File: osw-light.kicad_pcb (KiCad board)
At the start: 4 copper layers, 36.1 x 36.1 mm, 55 parts, among them J1 Conn_01x02, Q1 2N7002, SW1 SW_Push, SW2 SW_Push, SW4 SW_Push, SW5 SW_Push, U1 DS3231MZ, U10 XC6209, U11 MCP73831T-2ACI_OT, U13 XC6209, U2 BMA400, U4 GC9A01_IPS_display, U5 USB-OTG, U6 CH340E, U7 ttgo-32-micro, U9 TPS2115A

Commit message: Starting to add my modifications
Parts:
- removed C4: 0.1u, Capacitor_SMD:C_0603_1608Metric
- removed D1: LED_Green, LED_SMD:LED_0805_2012Metric
- removed G***: LOGO, footprints:p3dt_tiny
- removed G***: LOGO, footprints:aisler_15x12mm
- removed J1: Conn_01x02, Connector_PinHeader_2.54mm:PinHeader_1x02_P2.54mm_Vertical
- removed R13: 470R, Resistor_SMD:R_0603_1608Metric
- removed R15: 5k, Resistor_SMD:R_0603_1608Metric
- removed REF**: OSHW-Logo2_7.3x6mm_SilkScreen, Symbol:OSHW-Logo2_7.3x6mm_SilkScreen
- removed REF**: KiCad-Logo2_5mm_SilkScreen, Symbol:KiCad-Logo2_5mm_SilkScreen
- removed U11: MCP73831T-2ACI_OT, open-Smartwatch:SOT-23-5
- removed U7: ttgo-32-micro, open-Smartwatch:ttgo-32-micro
- removed U9: TPS2115A, open-Smartwatch:TSSOP-8_4.4x3mm_P0.65mm
- added J2: USB_C_Receptacle_USB2.0, Connector_USB:USB_C_Receptacle_GCT_USB4085, F.Cu at (73.1, 113.5)
- added R2: 5k1, Resistor_SMD:R_0603_1608Metric, F.Cu at (82.8, 112.3)
- added R3: 5k1, Resistor_SMD:R_0603_1608Metric, F.Cu at (74.7, 110.7)
- added R5: 10k, Resistor_SMD:R_0603_1608Metric, F.Cu at (65.6, 121.8)
- added TP1: BATT-VCC, TestPoint:TestPoint_Pad_3.0x3.0mm, F.Cu at (61.0, 104.1)
- added TP2: BATT-VCC, TestPoint:TestPoint_Pad_3.0x3.0mm, F.Cu at (61.0, 99.1)
- added U3: ESP32-PICO-MINI-02, open-Smartwatch:ESP32-PICO-MINI-02, F.Cu at (86.4, 101.6)
- C3: value 0.1u -> 1uF
- U1: value DS3231MZ -> RV-8523-C3; footprint Package_SO:SOIC-8_3.9x4.9mm_P1.27mm -> Package_SON:RTC_SMD_MicroCrystal_C3_2.5x3.7mm
- U5: value USB-OTG -> BQ24230RGT; footprint open-Smartwatch:USBmicro-B -> Package_DFN_QFN:VQFN-16-1EP_3x3mm_P0.5mm_EP1.68x1.68mm_ThermalVias
- moved C13 36.5 mm to (46.7, 110.7)
- moved C14 32.6 mm to (41.1, 99.5)
- moved U10 32.6 mm to (40.8, 96.7)
- moved C5 32.6 mm to (40.3, 101.4)
- moved R19 32.6 mm to (41.1, 103.4)
- moved C15 32.6 mm to (36.5, 99.5)
- moved C16 32.6 mm to (41.3, 94.0)
- moved C17 32.6 mm to (36.6, 94.0)
- moved C18 32.6 mm to (41.3, 92.4)
- moved C19 32.6 mm to (36.6, 92.4)
- moved C6 32.6 mm to (35.7, 101.4)
- moved R14 32.6 mm to (38.0, 103.4)
- moved U13 32.6 mm to (36.2, 96.7)
- moved C2 29.4 mm to (42.7, 116.6)
- moved C3 29.4 mm to (45.8, 116.6)
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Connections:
- C1 pad 2: /VBUS -> /VCC
- R14 pad 1: Net-(R14-Pad1) -> GND
- R14 pad 2: GND -> Net-(R14-Pad2)
- U1 pad 1: Net-(U1-Pad1) -> +3V3
- U1 pad 2: +3V3 -> /RTC_INT
- U1 pad 3: /RTC_INT -> /SCL
- U1 pad 4: Net-(U1-Pad4) -> /SDA
- U1 pad 5: GND -> unconnected-(U1-Pad5)
- U1 pad 6: +3V3 -> unconnected-(U1-Pad6)
- U1 pad 7: /SDA -> GND
- U1 pad 8: /SCL -> +3V3
- U10 pad 4: Net-(U10-Pad4) -> unconnected-(U10-Pad4)
- U13 pad 4: Net-(U13-Pad4) -> unconnected-(U13-Pad4)
- U2 pad 11: Net-(U2-Pad11) -> unconnected-(U2-Pad11)
- U2 pad 4: Net-(U2-Pad4) -> unconnected-(U2-Pad4)
- U5 pad 1: GND -> Net-(R5-Pad1)
- U5 pad 2: Net-(U5-Pad2) -> /VBAT
- U5 pad 3: /D_P -> /VBAT
- U5 pad 4: /D_N -> GND
- U5 pad 5: /VBUS -> GND
- U6 pad 4: Net-(U6-Pad4) -> unconnected-(U6-Pad4)
- U6 pad 5: Net-(U6-Pad5) -> unconnected-(U6-Pad5)
- U6 pad 6: Net-(U6-Pad6) -> unconnected-(U6-Pad6)
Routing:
- net +3V3: track 126.3 -> 13.5 mm, vias 11 -> 0
- net GND: track 64.5 -> 0.00 mm, vias 65 -> 0
- net /SCL: track 35.5 -> 0.00 mm, vias 3 -> 0
- net /VCC: track 30.7 -> 0.00 mm
- net /TFT_RST: track 29.6 -> 0.00 mm, vias 2 -> 0
- net /VBAT: track 29.5 -> 0.00 mm, vias 2 -> 0
- net /MOSI: track 28.4 -> 0.00 mm, vias 2 -> 0
- net /SDA: track 28.4 -> 0.00 mm, vias 3 -> 0
- net /B_MON: track 26.9 -> 0.00 mm, vias 2 -> 0
- net /EN: track 25.2 -> 0.00 mm, vias 6 -> 0
- net /BTN3: track 22.8 -> 0.00 mm, vias 3 -> 0
- net /VBUS: track 22.4 -> 0.00 mm
- net /SCK: track 22.0 -> 0.00 mm, vias 1 -> 0
- net /TFT_CS: track 20.6 -> 0.00 mm, vias 2 -> 0
- net /FLASH: track 20.0 -> 0.00 mm, vias 2 -> 0
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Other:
- net class Default removed

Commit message: Finalized layout
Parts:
- added C4: 0.1u, Capacitor_SMD:C_0603_1608Metric, F.Cu at (79.0, 84.8)
- added C7: 220nF, Capacitor_SMD:C_0603_1608Metric, F.Cu at (79.5, 89.4)
- added G***: LOGO, open-Smartwatch:new_707_logo_10x11, B.Cu at (88.9, 101.6)
- added G***: LOGO, footprints:p3dt_tiny, B.Cu at (76.2, 88.6)
- added REF**: KiCad-Logo2_6mm_SilkScreen, Symbol:KiCad-Logo2_6mm_SilkScreen, B.Cu at (76.2, 105.4)
- added U7: LSM303C, Package_LGA:LGA-12_2x2mm_P0.5mm, F.Cu at (79.5, 87.4)
- moved R19 43.1 mm to (82.5, 91.3), turned to 180 degrees
- moved C13 37.7 mm to (78.9, 91.0), turned to 0 degrees
- moved C6 34.2 mm to (69.8, 102.5), turned to 180 degrees
- moved C5 34.1 mm to (74.4, 102.5)
- moved C14 34.1 mm to (75.2, 100.5)
- moved C15 34.1 mm to (70.6, 100.5)
- moved U10 34.1 mm to (74.9, 97.7)
- moved U13 34.1 mm to (70.3, 97.7)
- moved C16 33.6 mm to (74.8, 94.7)
- moved C18 33.6 mm to (74.8, 93.2)
- moved C17 33.5 mm to (70.1, 94.7)
- moved C19 33.5 mm to (70.1, 93.2)
- moved R14 30.0 mm to (67.8, 106.7), turned to -90 degrees
- moved C3 27.2 mm to (70.7, 105.5)
- moved C2 23.7 mm to (64.3, 106.7), turned to 90 degrees
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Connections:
- R19 pad 1: /VCC -> +3V3
- SW2 pad 1: /BTN3 -> +3V3
- SW2 pad 2: +3V3 -> /BTN3
- U2 pad 5: /IO34 -> /IO35
- U2 pad 6: /IO35 -> /IO34
- U3 pad 6: /STAT_PWR -> /DRDY_MAG
- U3 pad 7: unconnected-(U3-Pad7) -> /STAT_PWR
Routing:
- net +3V3: track 13.5 -> 103.5 mm, vias 0 -> 6
- net /SCL: track 0.00 -> 49.3 mm, vias 0 -> 4
- net /SDA: track 0.00 -> 44.4 mm, vias 0 -> 5
- net /VCC: track 0.00 -> 40.4 mm, vias 0 -> 3
- net /STAT_PWR: track 0.00 -> 36.4 mm, vias 0 -> 3
- net /TFT_CS: track 0.00 -> 34.4 mm, vias 0 -> 2
- net /BTN2: track 0.00 -> 33.3 mm, vias 0 -> 2
- net /MOSI: track 0.00 -> 31.2 mm, vias 0 -> 2
- net /VBAT: track 0.00 -> 30.2 mm, vias 0 -> 2
- net /FLASH: track 0.00 -> 28.2 mm, vias 0 -> 2
- net /PIN_LED: track 0.00 -> 27.4 mm, vias 0 -> 2
- net /TFT_RST: track 0.00 -> 27.1 mm, vias 0 -> 2
- net /SCK: track 0.00 -> 27.0 mm, vias 0 -> 2
- net /TFT_DC: track 0.00 -> 26.1 mm, vias 0 -> 2
- net /EN: track 0.00 -> 23.6 mm, vias 0 -> 2
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
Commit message: Started working on LoRa version/changes
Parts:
- removed REF**: KiCad-Logo2_6mm_SilkScreen, Symbol:KiCad-Logo2_6mm_SilkScreen
- added AE1: Antenna, Connector_Coaxial:U.FL_Molex_MCRF_73412-0110_Vertical, F.Cu at (69.8, 93.2)
- added AE2: Antenna, Connector_PinHeader_2.54mm:PinHeader_1x01_P2.54mm_Vertical, F.Cu at (76.2, 84.8)
- added C10: 0.1u, Capacitor_SMD:C_0603_1608Metric, B.Cu at (83.9, 90.2)
- added U8: RFM95W-868S2, RF_Module:HOPERF_RFM9XW_SMD, B.Cu at (83.0, 101.0)
- moved R18 7.87 mm to (79.8, 96.0), turned to 90 degrees
- moved C19 6.52 mm to (65.8, 98.0), turned to 135 degrees
- moved C17 3.84 mm to (66.9, 96.9), turned to 135 degrees
- moved G*** 3.81 mm to (85.1, 101.6)
- moved U1 2.37 mm to (74.8, 89.1)
- moved C11 2.37 mm to (72.1, 88.3)
- moved R21 2.07 mm to (61.3, 95.5)
- moved Q1 2.07 mm to (62.2, 99.0)
- moved R22 2.07 mm to (63.0, 95.5)
- moved C4 0.77 mm to (79.8, 85.0)
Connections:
- U3 pad 19: /TFT_DC -> /MISO
- U3 pad 21: unconnected-(U3-Pad21) -> /TFT_DC
- U3 pad 26: unconnected-(U3-Pad26) -> /LORA_IO0
- U3 pad 27: unconnected-(U3-Pad27) -> /LORA_CS
- U3 pad 28: unconnected-(U3-Pad28) -> /LORA_RST
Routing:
- net /SCL: track 49.3 -> 1.73 mm, vias 4 -> 0
- net +3V3: track 103.5 -> 72.2 mm, vias 6 -> 3
- net /SDA: track 44.4 -> 14.0 mm, vias 5 -> 0
- net /TFT_DC: track 26.1 -> 4.87 mm, vias 2 -> 0
- net /MISO: track 0.00 -> 21.3 mm, vias 0 -> 1
- net /DRDY_MAG: track 17.9 -> 0.00 mm, vias 2 -> 0
- net /EN: track 23.6 -> 7.30 mm, vias 2 -> 1
- net /RTC_INT: track 20.0 -> 5.28 mm, vias 2 -> 1
- net GND: track 19.9 -> 9.69 mm, vias 39 -> 30
- net /STAT_PWR: track 36.4 -> 29.4 mm, vias 3 -> 2
- net /BTN3: track 12.1 -> 7.92 mm
- net /3V3_2: track 16.9 -> 13.5 mm
- net /TFT_RST: track 27.1 -> 30.5 mm
- net /TFT_CS: track 34.4 -> 37.2 mm, vias 2 -> 1
- net /MOSI: track 31.2 -> 34.0 mm
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
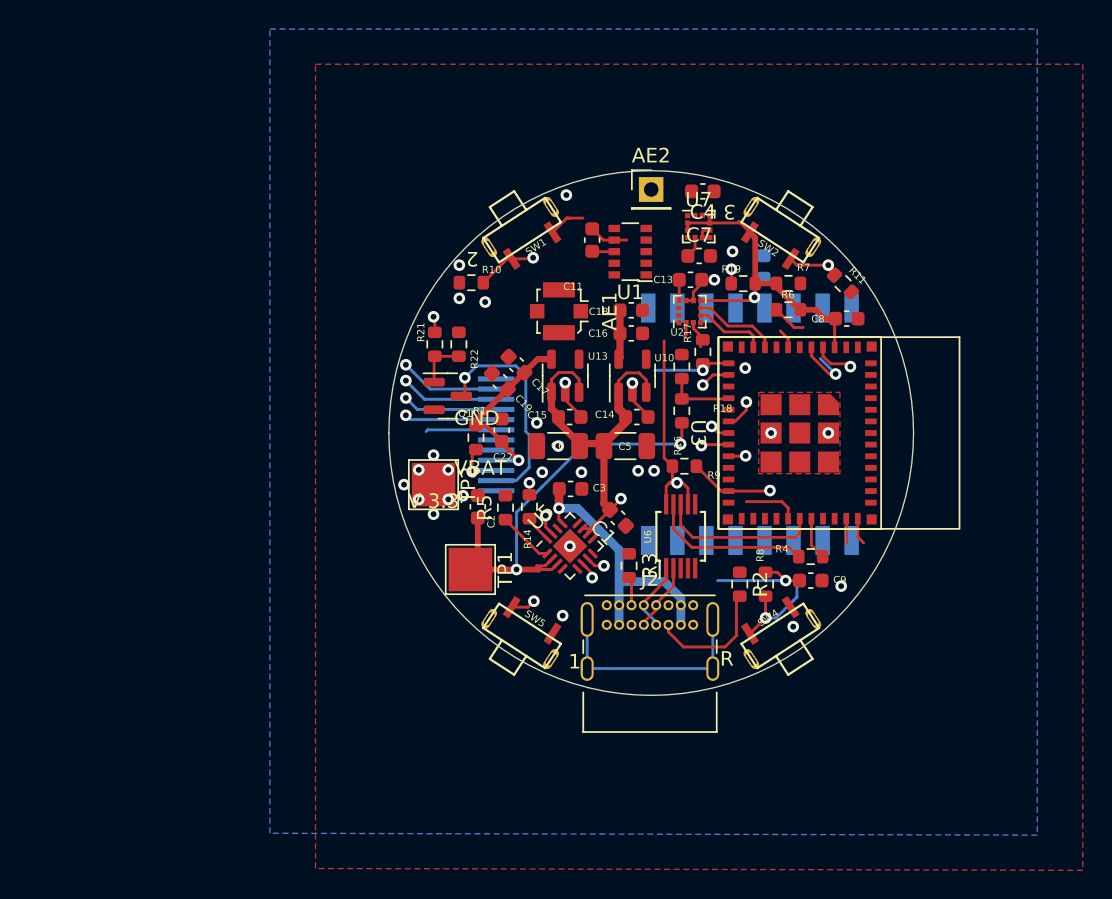
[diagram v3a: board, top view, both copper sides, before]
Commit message: Layed out board. Changed a duplicate sensor for a temperature one
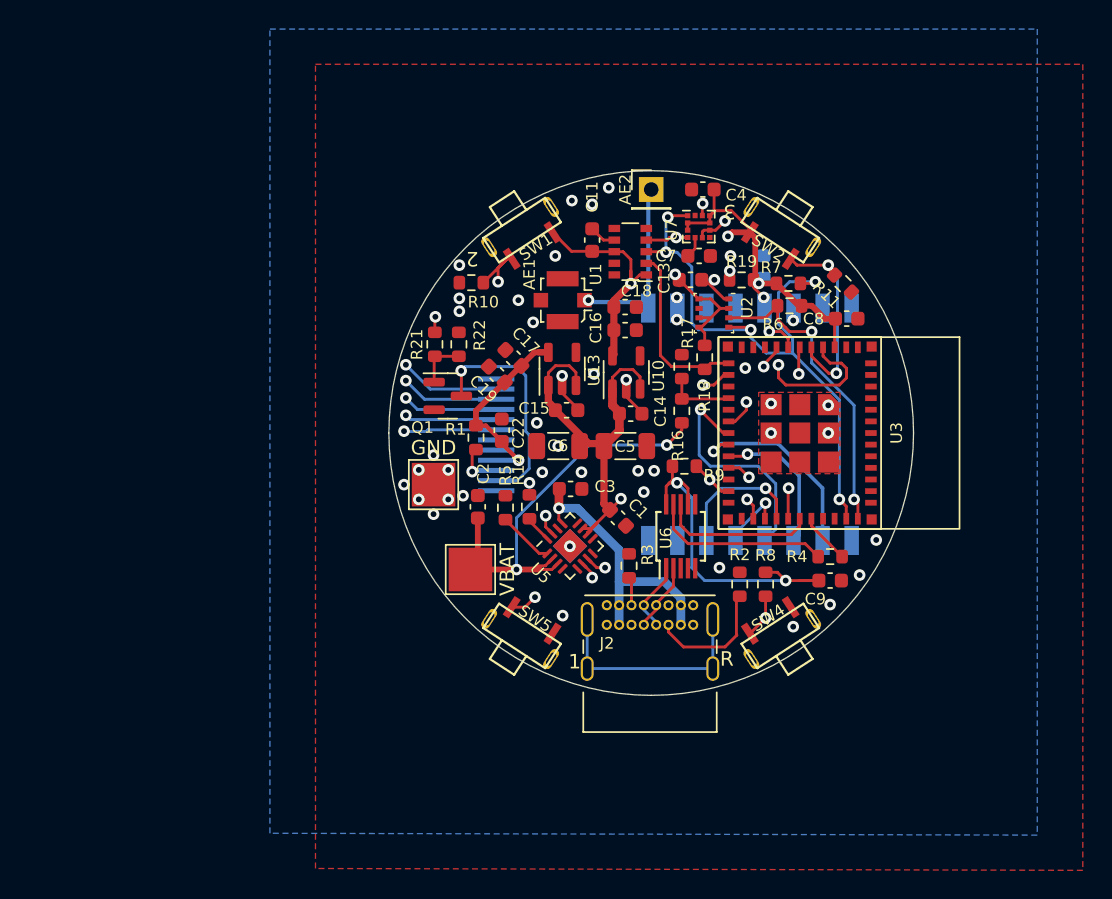
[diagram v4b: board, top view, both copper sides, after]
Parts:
- J2: value USB_C_Receptacle_USB2.0 -> GCT_USB4085
- U2: value BMA400 -> BME280; footprint open-Smartwatch:LGA-12_2x2mm_P0.5mm -> Package_LGA:Bosch_LGA-8_2.5x2.5mm_P0.65mm_ClockwisePinNumbering
- moved U2 1.67 mm to (80.5, 93.3), turned to -90 degrees
- moved C9 1.33 mm to (88.5, 111.8)
- moved R4 1.33 mm to (88.5, 110.1)
- moved G*** 1.02 mm to (86.1, 101.6)
- moved AE1 0.80 mm to (70.1, 92.5)
- moved C15 0.52 mm to (70.4, 100.0)
- moved C17 0.52 mm to (66.7, 96.4)
- moved C19 0.52 mm to (65.6, 97.6)
- moved U13 0.52 mm to (70.1, 97.2)
- moved C16 0.48 mm to (74.4, 94.5)
- moved C14 0.48 mm to (74.8, 100.3)
- moved C18 0.48 mm to (74.4, 92.9)
- moved U10 0.48 mm to (74.5, 97.4)
- moved R18 0.40 mm to (79.9, 96.4)
- moved R6 0.29 mm to (85.7, 92.8)
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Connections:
- AE1 pad 2: (no net) -> GND
- U2 pad 2: /SDA -> +3V3
- U2 pad 3: +3V3 -> /SDA
- U2 pad 4: unconnected-(U2-Pad4) -> /SCL
- U2 pad 5: /IO35 -> +3V3
- U2 pad 6: /IO34 -> +3V3
- U2 pad 7: +3V3 -> GND
- U2 pad 8: GND -> +3V3
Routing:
- net /SCL: track 1.73 -> 42.5 mm, vias 0 -> 5
- net /TFT_DC: track 4.87 -> 33.1 mm, vias 0 -> 2
- net +3V3: track 72.2 -> 100.0 mm, vias 3 -> 7
- net /SDA: track 14.0 -> 39.6 mm, vias 0 -> 3
- net /LORA_IO0: track 0.00 -> 19.4 mm, vias 0 -> 2
- net /DRDY_MAG: track 0.00 -> 18.2 mm, vias 0 -> 2
- net /EN: track 7.30 -> 25.4 mm, vias 1 -> 2
- net /SCK: track 29.8 -> 44.2 mm
- net Net-(AE1-Pad1): track 0.00 -> 13.4 mm, vias 0 -> 1
- net /LORA_RST: track 0.00 -> 9.47 mm, vias 0 -> 1
- net /MOSI: track 34.0 -> 43.1 mm
- net /MISO: track 21.3 -> 13.8 mm
- net /RTC_INT: track 5.28 -> 11.9 mm, vias 1 -> 0
- net /BTN3: track 7.92 -> 14.2 mm
- net /IO34: track 5.88 -> 0.00 mm
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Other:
- board text added: "OpenSmartWatch E707 LORA Edition Rev 1.0"
- board text removed: "V 3.3"

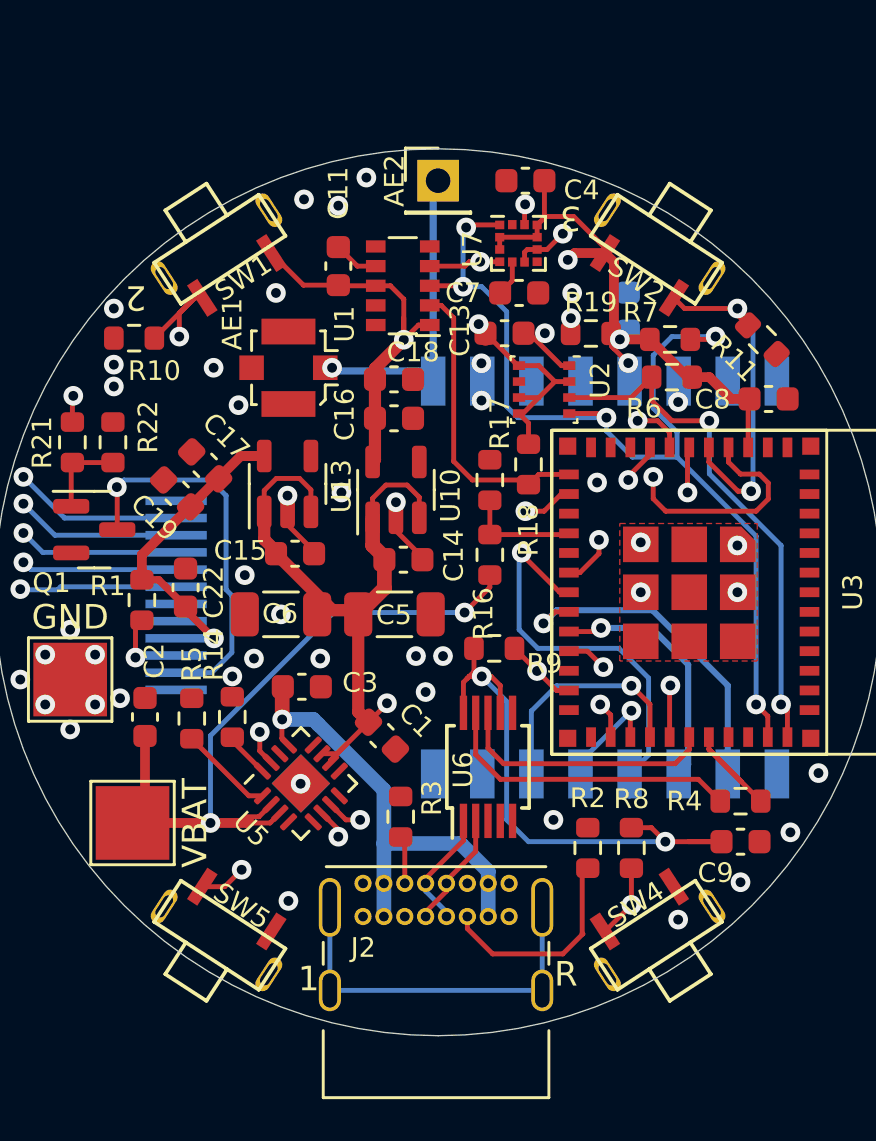
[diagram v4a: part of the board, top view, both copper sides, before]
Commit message: Changed switch to proper one
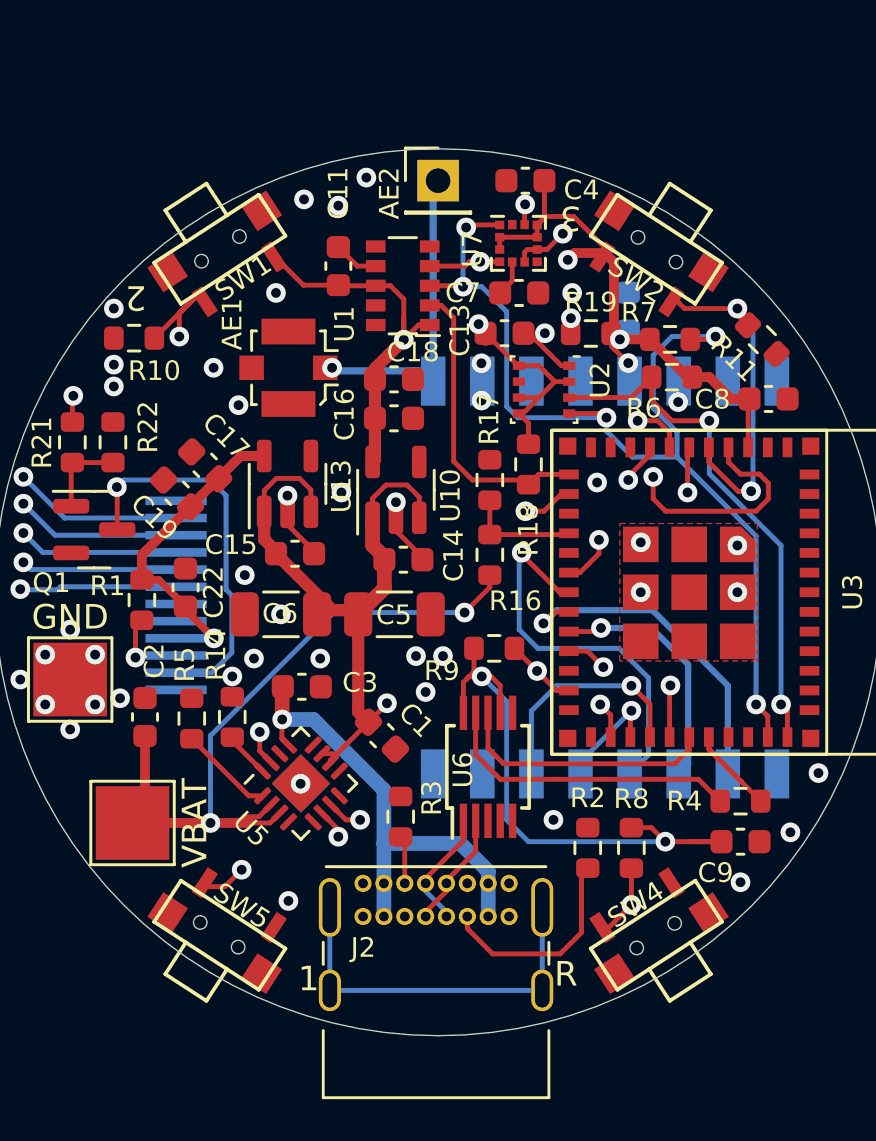
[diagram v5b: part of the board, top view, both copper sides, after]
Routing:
- net GND: vias 45 -> 44
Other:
- rule pad_to_mask_clearance: 0.051 -> 0
